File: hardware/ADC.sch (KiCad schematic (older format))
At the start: 4 parts, among them J4 691327310016, J5 691327310016, U1 ADS8556IPM, U2 OPA2211AIDDA

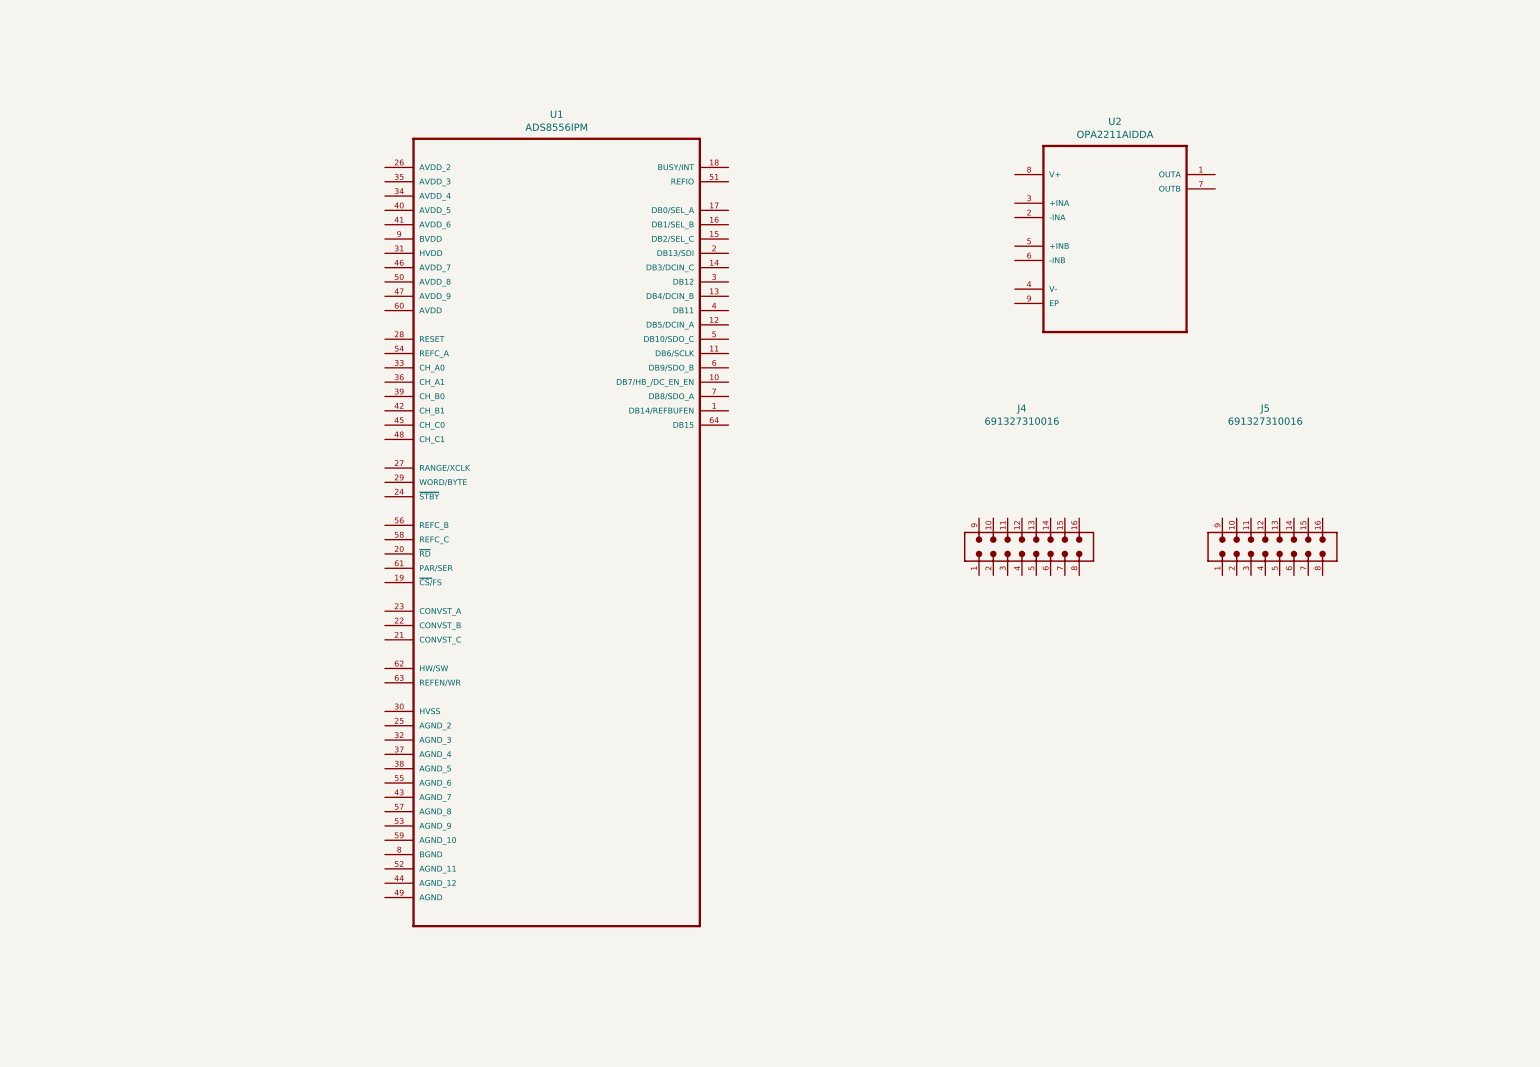
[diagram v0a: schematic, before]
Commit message: Adding decoupling capacitors, termination resoistors for LVDS IN
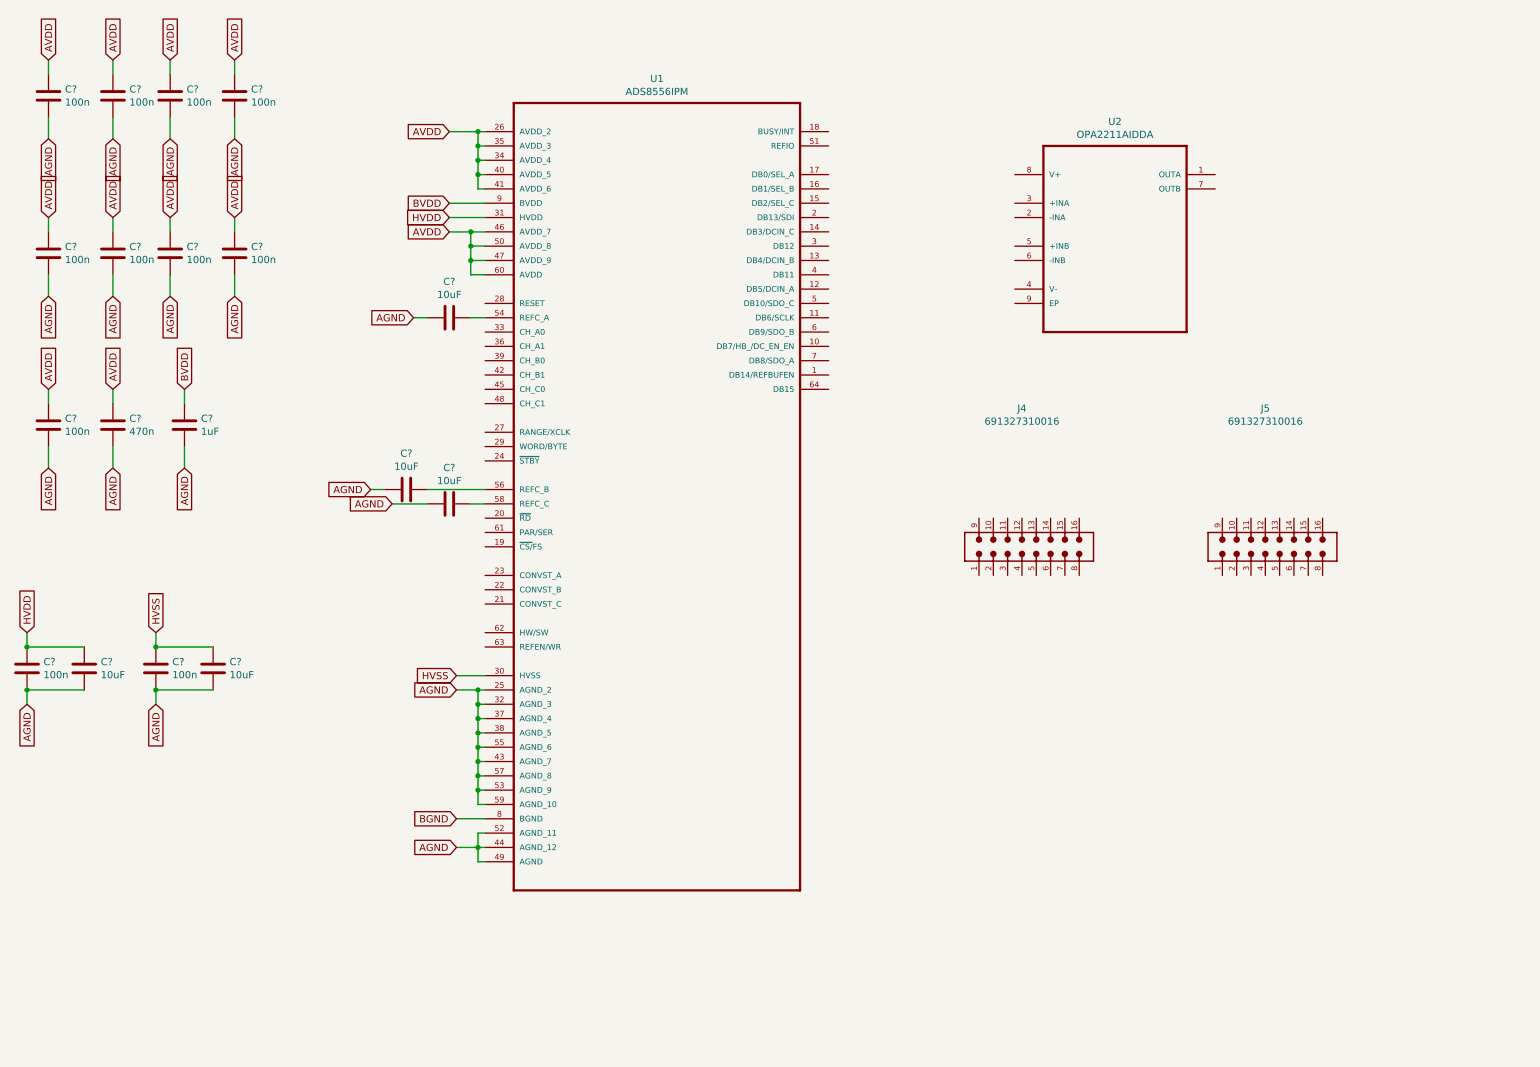
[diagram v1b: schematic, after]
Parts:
- added C? (x11): 100n, symbol antena:C
- added C? (x5): 10uF, symbol antena:C
- added C?: 470n, symbol antena:C
- added C?: 1uF, symbol antena:C
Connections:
- net AGND: now reaches U1.25 (AGND_2)
- net AGND: now also U1.32 (AGND_3), U1.37 (AGND_4), U1.38 (AGND_5), U1.43 (AGND_7), U1.44 (AGND_12), U1.49 (AGND), U1.52 (AGND_11), U1.53 (AGND_9), U1.55 (AGND_6), U1.57 (AGND_8), U1.59 (AGND_10), C?.1, C?.1, C?.1, C?.2, C?.2, C?.2, C?.2, C?.2, C?.2, C?.2, C?.2, C?.2, C?.2, C?.2, C?.2, C?.2, C?.2, C?.2
- net AVDD: now reaches U1.26 (AVDD_2)
- net AVDD: now also U1.34 (AVDD_4), U1.35 (AVDD_3), U1.40 (AVDD_5), U1.41 (AVDD_6), U1.46 (AVDD_7), U1.47 (AVDD_9), U1.50 (AVDD_8), U1.60 (AVDD), C?.1, C?.1, C?.1, C?.1, C?.1, C?.1, C?.1, C?.1, C?.1, C?.1
- net HVSS: now reaches U1.30 (HVSS)
- net HVSS: now also C?.1, C?.1
- net HVDD: now reaches U1.31 (HVDD)
- net HVDD: now also C?.1, C?.1
- net at U1.54 (REFC_A): now also C?.2
- net at U1.56 (REFC_B): now also C?.2
- net at U1.58 (REFC_C): now also C?.2
- net BGND: now reaches U1.8 (BGND)
- net BVDD: now reaches U1.9 (BVDD)
- net BVDD: now also C?.1
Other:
- moved on the sheet: U1

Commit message: Adding selection resistors
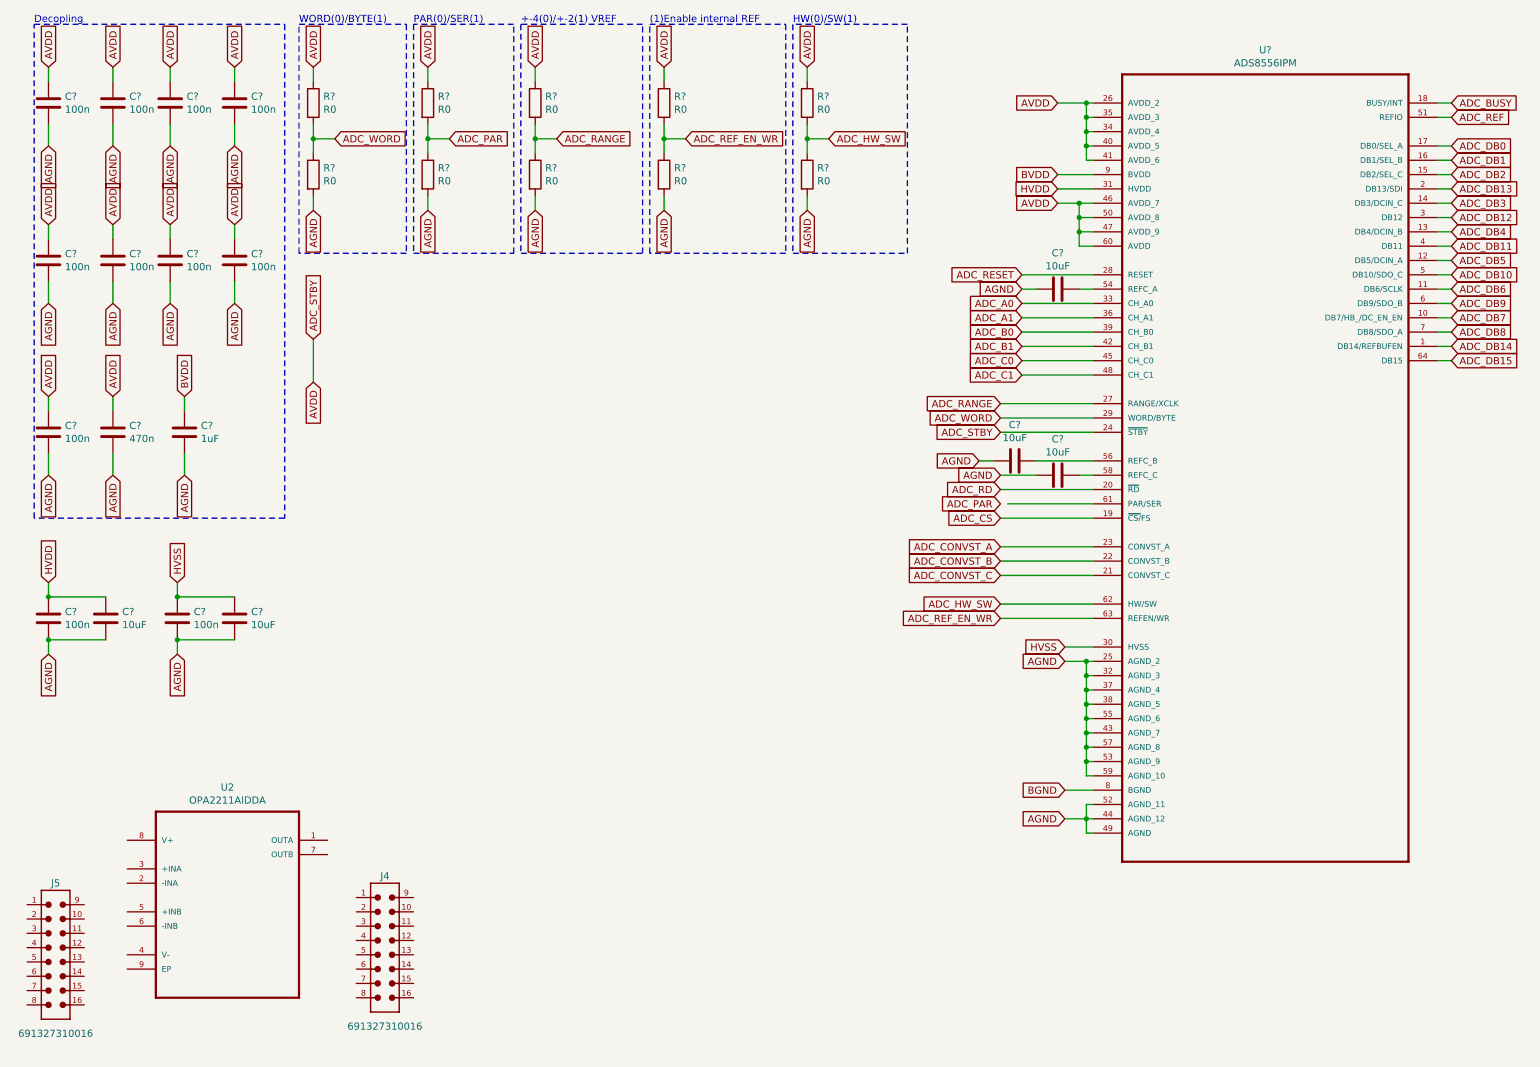
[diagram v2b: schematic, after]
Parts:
- removed U1: ADS8556IPM, ADS8556IPM:QFP50P1200X1200X160-64N, symbol ADS8556IPM:ADS8556IPM
- added R? (x10): R0, symbol antena:R
- added U?: ADS8556IPM, QFP50P1200X1200X160-64N, symbol ADS8556IPM:ADS8556IPM
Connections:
- net AGND: now also R?.2, R?.2, R?.2, R?.2, R?.2, U?.25 (AGND_2), U?.32 (AGND_3), U?.37 (AGND_4), U?.38 (AGND_5), U?.43 (AGND_7), U?.44 (AGND_12), U?.49 (AGND), U?.52 (AGND_11), U?.53 (AGND_9), U?.55 (AGND_6), U?.57 (AGND_8), U?.59 (AGND_10)
- net BGND: now also U?.8 (BGND)
- net BVDD: now also U?.9 (BVDD)
- net HVDD: now also U?.31 (HVDD)
- net HVSS: now also U?.30 (HVSS)
- net at C?.2: now also U?.54 (REFC_A)
- net at C?.2: now also U?.56 (REFC_B)
- net at C?.2: now also U?.58 (REFC_C)
- net AVDD renamed ADC_STBY
- net ADC_STBY: now also R?.1, R?.1, R?.1, R?.1, R?.1, U?.24 (~STBY), U?.26 (AVDD_2), U?.34 (AVDD_4), U?.35 (AVDD_3), U?.40 (AVDD_5), U?.41 (AVDD_6), U?.46 (AVDD_7), U?.47 (AVDD_9), U?.50 (AVDD_8), U?.60 (AVDD)
- new net ADC_A0: U?.33 (CH_A0)
- new net ADC_A1: U?.36 (CH_A1)
- new net ADC_B0: U?.39 (CH_B0)
- new net ADC_B1: U?.42 (CH_B1)
- new net ADC_BUSY: U?.18 (BUSY/INT)
- new net ADC_C0: U?.45 (CH_C0)
- new net ADC_C1: U?.48 (CH_C1)
- new net ADC_CONVST_A: U?.23 (CONVST_A)
- new net ADC_CONVST_B: U?.22 (CONVST_B)
- new net ADC_CONVST_C: U?.21 (CONVST_C)
- new net ADC_CS: U?.19 (~CS/~FS)
- new net ADC_DB0: U?.17 (DB0/SEL_A)
- new net ADC_DB1: U?.16 (DB1/SEL_B)
- new net ADC_DB10: U?.5 (DB10/SDO_C)
- new net ADC_DB11: U?.4 (DB11)
- new net ADC_DB12: U?.3 (DB12)
- new net ADC_DB13: U?.2 (DB13/SDI)
- new net ADC_DB14: U?.1 (DB14/REFBUFEN)
- new net ADC_DB15: U?.64 (DB15)
- new net ADC_DB2: U?.15 (DB2/SEL_C)
- new net ADC_DB3: U?.14 (DB3/DCIN_C)
- new net ADC_DB4: U?.13 (DB4/DCIN_B)
- new net ADC_DB5: U?.12 (DB5/DCIN_A)
- new net ADC_DB6: U?.11 (DB6/SCLK)
- new net ADC_DB7: U?.10 (DB7/HB_/DC_EN_EN)
- new net ADC_DB8: U?.7 (DB8/SDO_A)
- new net ADC_DB9: U?.6 (DB9/SDO_B)
- new net ADC_HW_SW: R?.1, R?.2, U?.62 (HW/SW)
- new net ADC_PAR: R?.1, R?.2
- new net ADC_RANGE: R?.1, R?.2, U?.27 (RANGE/XCLK)
- new net ADC_RD: U?.20 (~RD)
- new net ADC_REF: U?.51 (REFIO)
- new net ADC_REF_EN_WR: R?.1, R?.2, U?.63 (REFEN/WR)
- new net ADC_RESET: U?.28 (RESET)
- new net ADC_WORD: R?.1, R?.2, U?.29 (WORD/BYTE)
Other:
- note added: "(1)Enable internal REF"
- note added: "+-4(0)/+-2(1) VREF"
- note added: "Decopling"
- note added: "HW(0)/SW(1)"
- note added: "PAR(0)/SER(1)"
- note added: "WORD(0)/BYTE(1)"
- moved on the sheet: C?, J4, J5, U2

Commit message: Adding buffe ramp , REF amp, DIFF amp
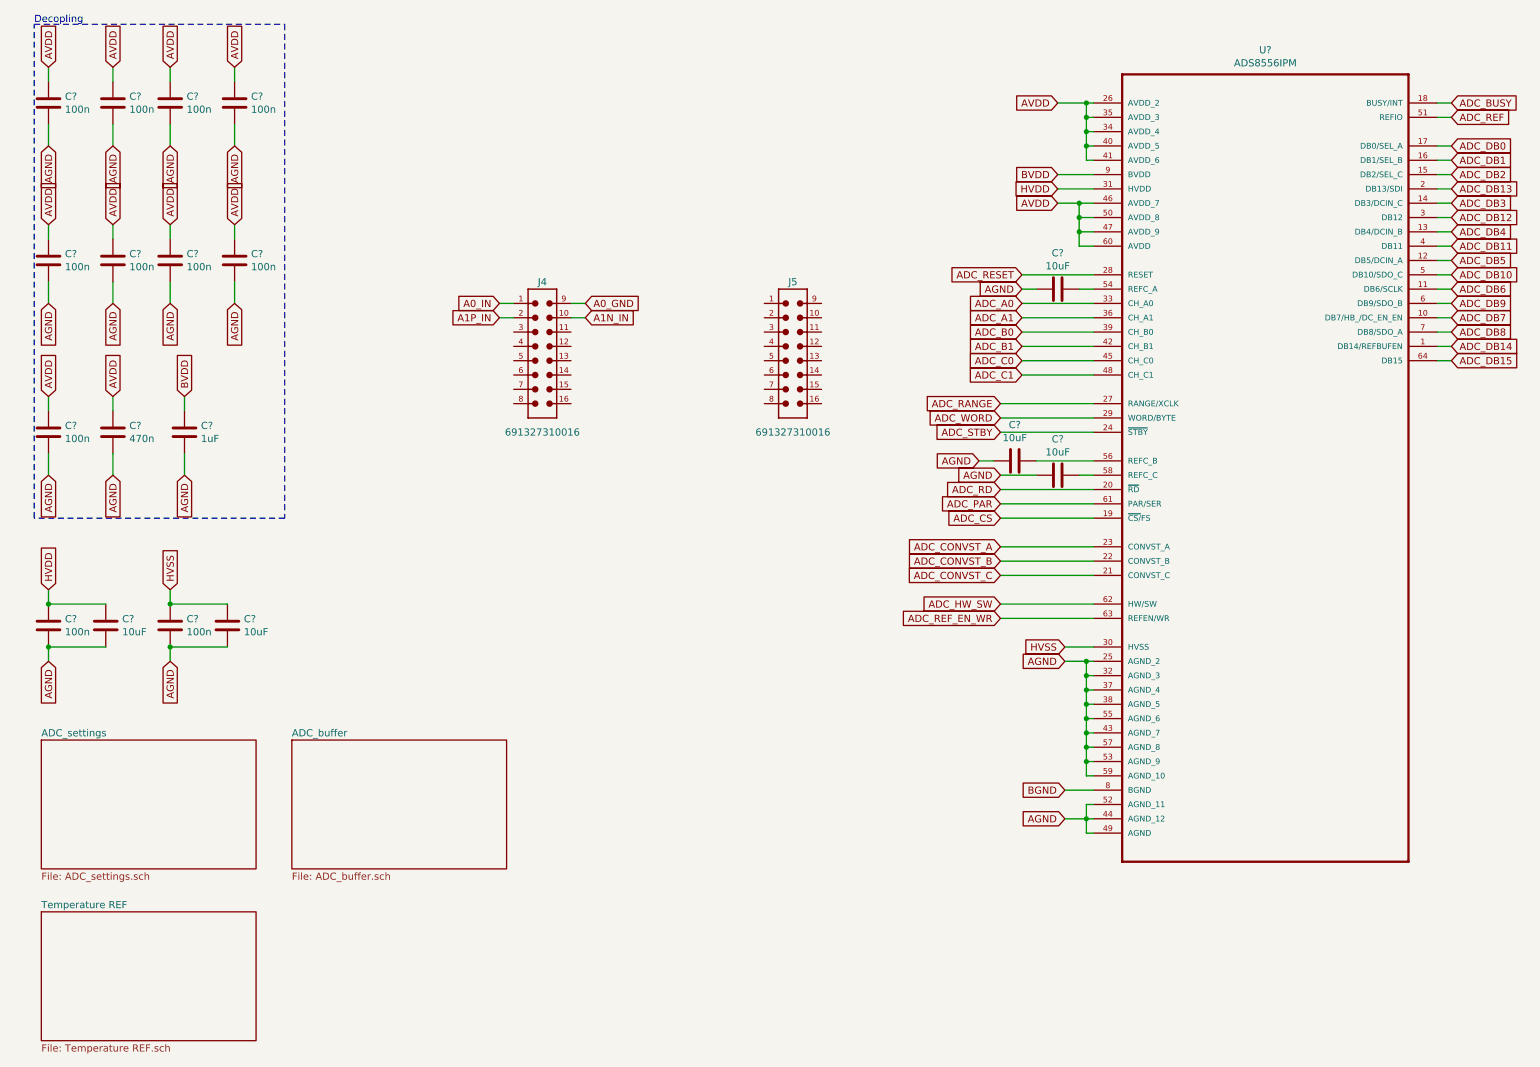
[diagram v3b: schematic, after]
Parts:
- removed R? (x10): R0, symbol antena:R
- removed U2: OPA2211AIDDA, OPA2211:SOIC127P600X170-9N, symbol OPA2211AIDDA:OPA2211AIDDA
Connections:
- net ADC_PAR: now also U?.61 (PAR/SER)
- net ADC_STBY: no longer C?.1, C?.1, C?.1, C?.1, C?.1, C?.1, C?.1, C?.1, C?.1, C?.1, U?.26 (AVDD_2), U?.34 (AVDD_4), U?.35 (AVDD_3), U?.40 (AVDD_5), U?.41 (AVDD_6), U?.46 (AVDD_7), U?.47 (AVDD_9), U?.50 (AVDD_8), U?.60 (AVDD)
- net A0_IN: now reaches J4.1
- net A1N_IN: now reaches J4.10
- net A1P_IN: now reaches J4.2
- net A0_GND: now reaches J4.9
- new net AVDD: C?.1, C?.1, C?.1, C?.1, C?.1, C?.1, C?.1, C?.1, C?.1, C?.1, U?.26 (AVDD_2), U?.34 (AVDD_4), U?.35 (AVDD_3), U?.40 (AVDD_5), U?.41 (AVDD_6), U?.46 (AVDD_7), U?.47 (AVDD_9), U?.50 (AVDD_8), U?.60 (AVDD)
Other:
- note removed: "(1)Enable internal REF"
- note removed: "+-4(0)/+-2(1) VREF"
- note removed: "HW(0)/SW(1)"
- note removed: "PAR(0)/SER(1)"
- note removed: "WORD(0)/BYTE(1)"
- moved on the sheet: C?, J4, J5

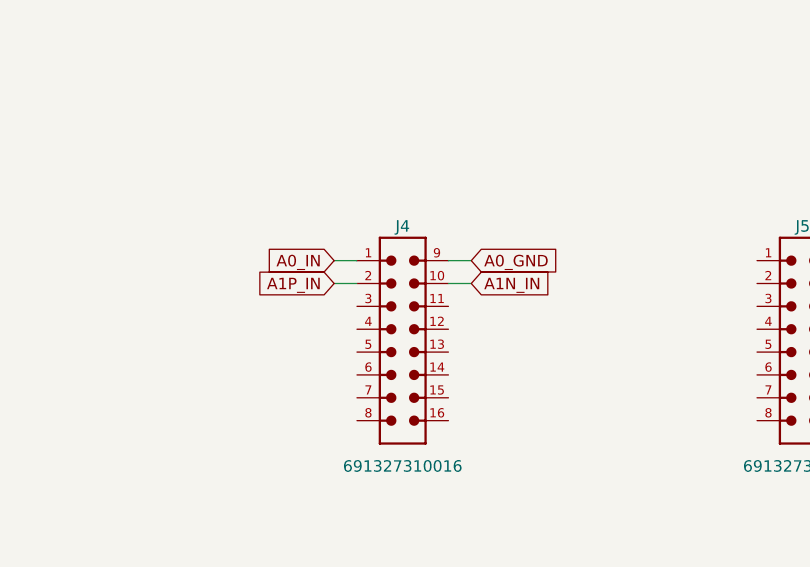
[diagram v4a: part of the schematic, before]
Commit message: Adding ULX3S connections
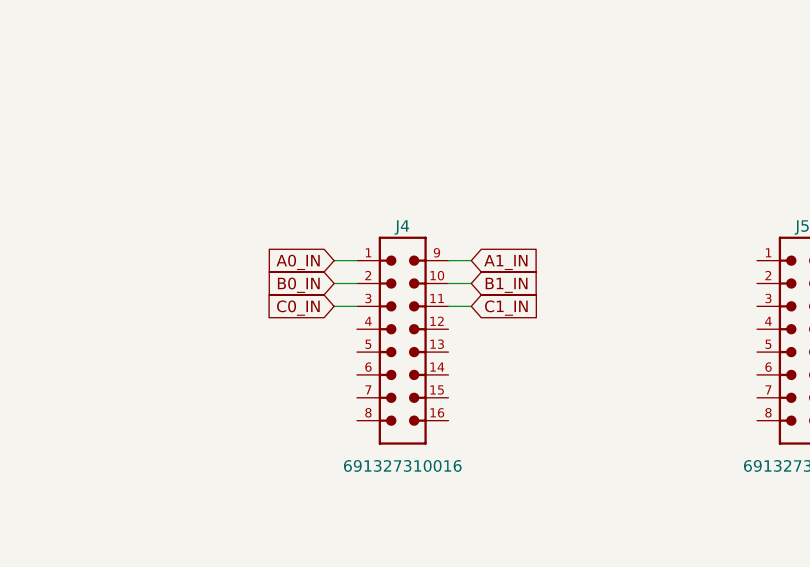
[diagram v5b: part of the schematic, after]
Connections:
- net C1_IN: now reaches J4.11
- net C0_IN: now reaches J4.3
- net A0_GND renamed A1_IN
- net A1N_IN renamed B1_IN
- net A1P_IN renamed B0_IN
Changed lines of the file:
@@
 A0_IN
 Text GLabel 4600 2550 2    50   Input ~ 0
-A0_GND
+A1_IN
 Wire Wire Line
 	4500 2550 4600 2550
@@
 	4000 2550 4100 2550
 Text GLabel 4000 2650 0    50   Input ~ 0
-A1P_IN
+B0_IN
 Text GLabel 4600 2650 2    50   Input ~ 0
-A1N_IN
+B1_IN
 Wire Wire Line
 	4600 2650 4500 2650
@@
 Wire Wire Line
 	7500 3950 8150 3950
+Text GLabel 4000 2750 0    50   Input ~ 0
+C0_IN
+Text GLabel 4600 2750 2    50   Input ~ 0
+C1_IN
+Wire Wire Line
+	4600 2750 4500 2750
+Wire Wire Line
+	4000 2750 4100 2750
 $EndSCHEMATC
